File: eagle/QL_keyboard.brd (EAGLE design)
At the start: 66 x 51.4 mm, 40 parts, among them J1 USB-A-S, J2 AVR_SPI_PRG_6TESTPOINTS, U2 3.3V/150mA, U3 MAX3421ESMD, U4 ATMEGA328P_TQFP, U5 TXB0108PW-TSSOP20, Y1 8MHZ

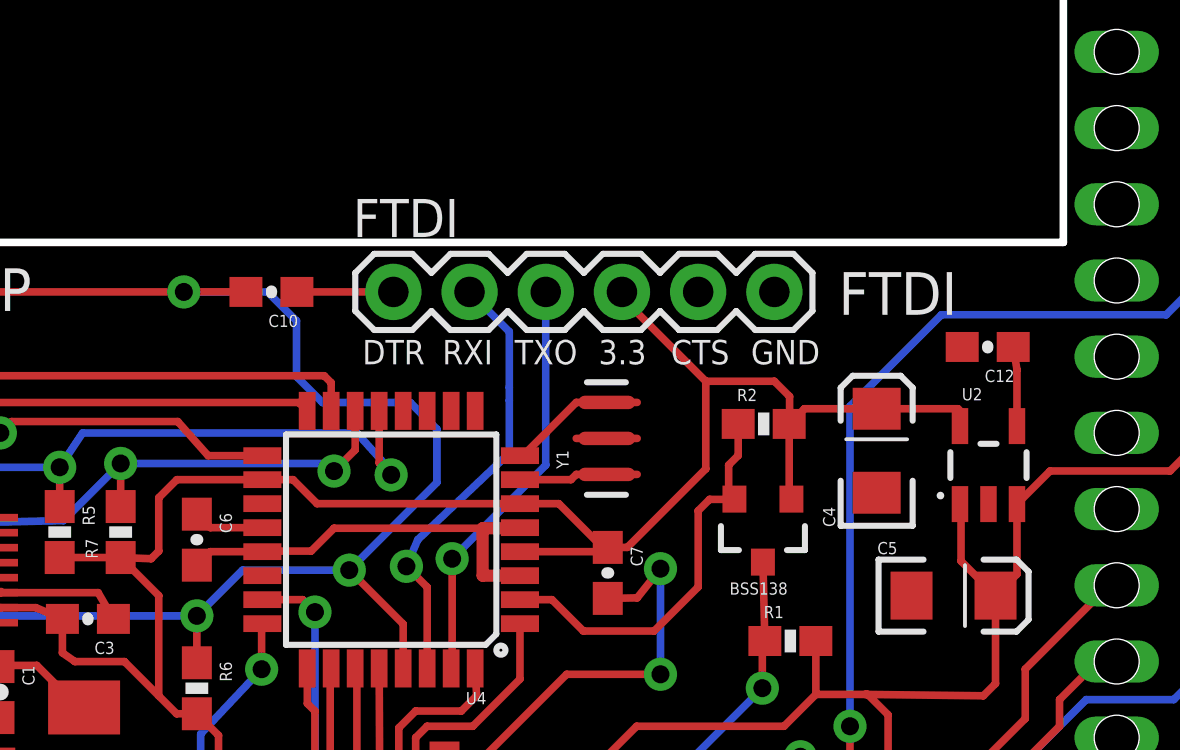
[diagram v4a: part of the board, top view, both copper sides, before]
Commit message: Replace FTDI header with a two pin RXI/TXO header.
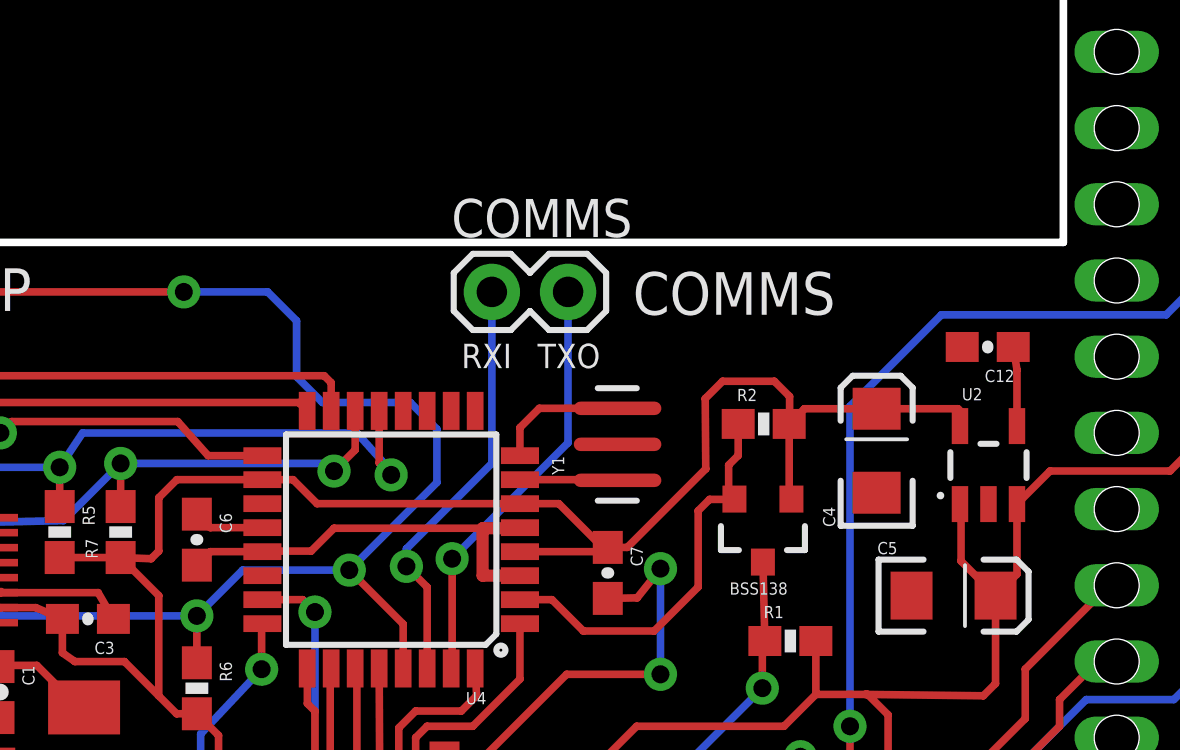
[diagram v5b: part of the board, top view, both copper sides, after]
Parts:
- removed C10: 0.1uF, SparkFun-Capacitors:0603-CAP
- removed FTDI: 1, SparkFun-Connectors:1X06
- added COMMS: (no value), ppe_custom:1X02
- Y1: device SparkFun-FreqCtrl:RESONATOR-SMD -> ppe_custom:RESONATOR-SMD
- moved Y1 0.41 mm to (46.1, 26.5)
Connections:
- removed net DTR: C10.1, FTDI.1
- net 3.3V: no longer FTDI.4
- net GND: no longer FTDI.5, FTDI.6
- net RST: no longer C10.2
- net RXI: now also COMMS.1; no longer FTDI.2
- net TXO: now also COMMS.2; no longer FTDI.3
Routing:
- net 3.3V: track 93.9 -> 89.4 mm
- net DTR: track 3.21 -> 0.00 mm
- net RST: track 57.0 -> 55.0 mm
- net N$15: track 2.61 -> 4.45 mm
- net N$16: track 1.98 -> 3.26 mm
- net RXI: track 14.8 -> 14.0 mm
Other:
- board text added: "COMMS"
- board text removed: "CTS"
- board text removed: "DTR"
- board text removed: "FTDI"

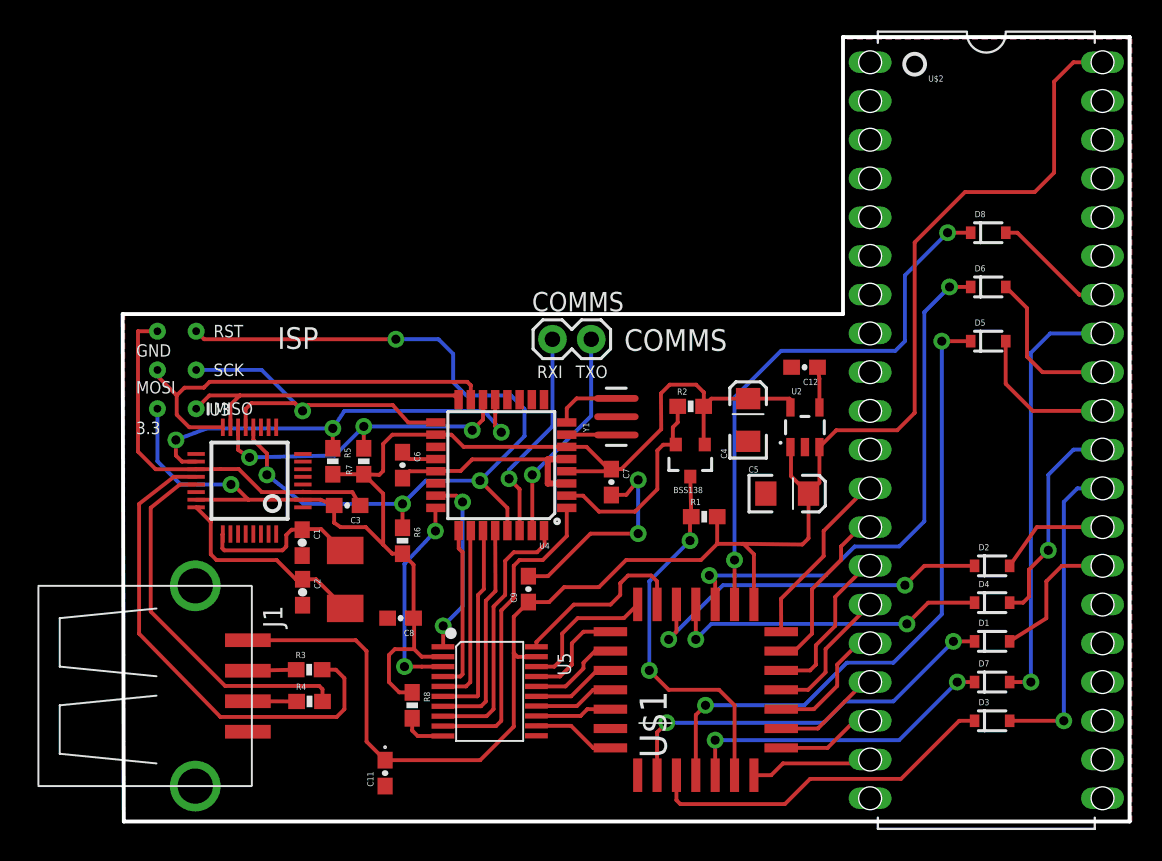
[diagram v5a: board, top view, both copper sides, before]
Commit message: Move ISP header and fix USB connector footprint
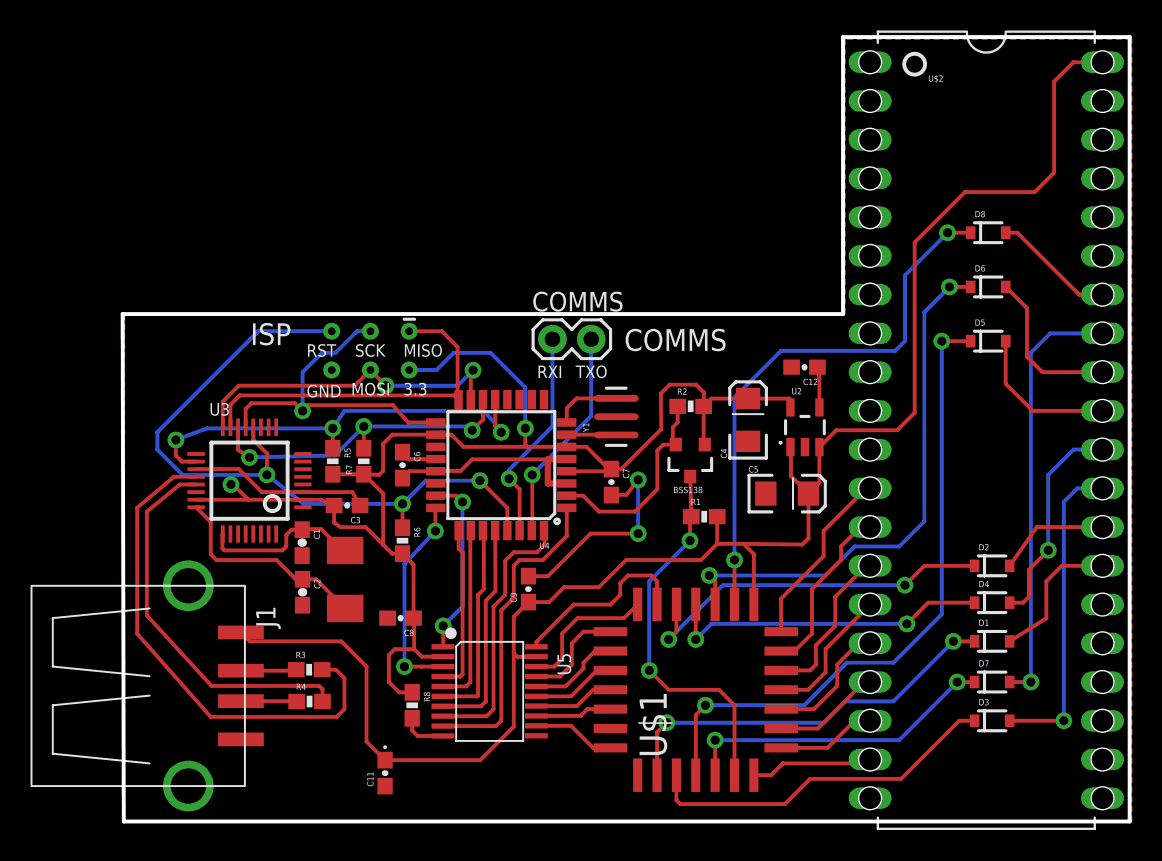
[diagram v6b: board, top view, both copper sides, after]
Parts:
- J1: device SparkFun-Connectors:USB-A-S -> ppe_custom:USB-A-S
- moved J2 12.8 mm to (30.0, 30.9), turned to 180 degrees
- moved J1 0.45 mm to (18.0, 8.89)
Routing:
- net GND: track 53.6 -> 40.2 mm
- net RST: track 55.0 -> 47.5 mm, vias 4 -> 3
- net MOSI: track 27.5 -> 21.8 mm, vias 0 -> 2
- net 3.3V: track 89.4 -> 93.5 mm, vias 1 -> 2
- net MISO: track 20.0 -> 23.9 mm
- net N$3: track 24.5 -> 25.1 mm

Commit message: General cleanup of layout
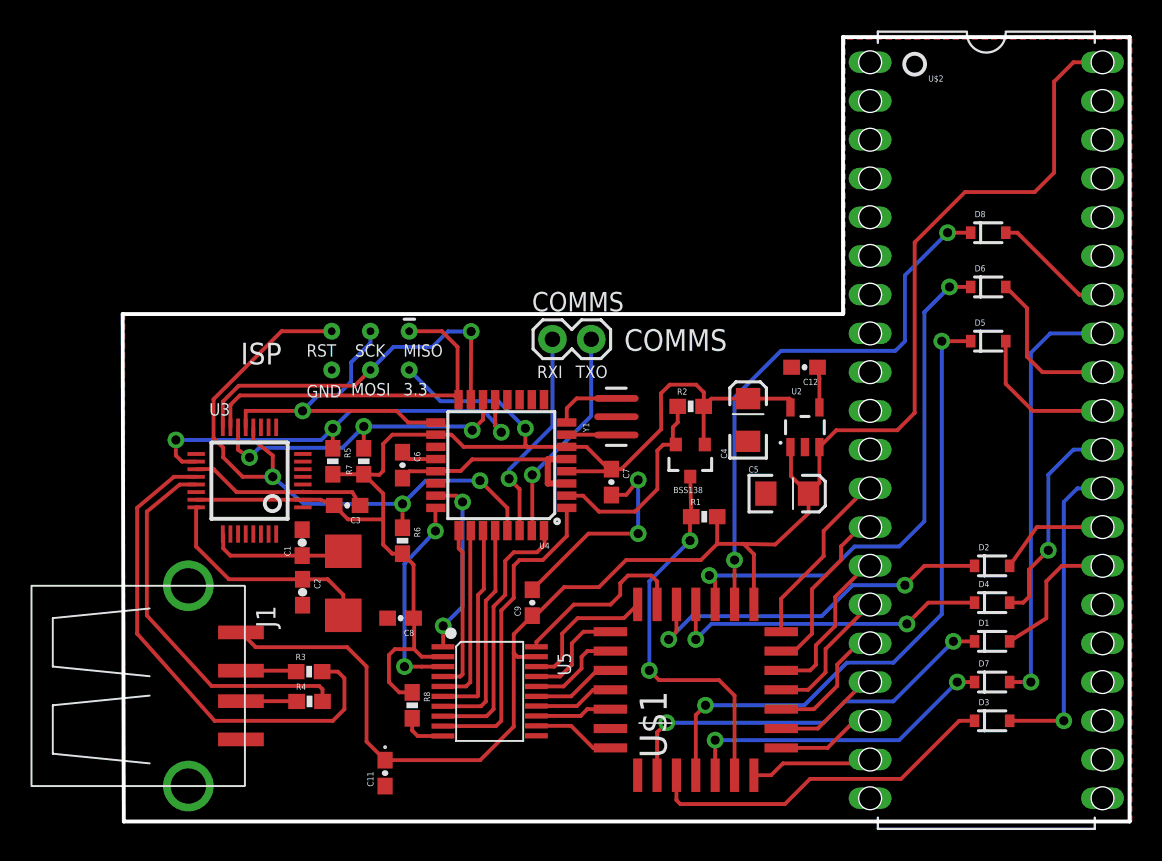
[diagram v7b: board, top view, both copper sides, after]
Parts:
- removed XTAL-12MHZ: CRYSTAL-SMD, ppe_custom:CRYSTAL-SMD-5X3.2
- added U$3: CRYSTAL-SMD, ppe_custom:CRYSTAL-SMD-5X3.2
- moved C9 0.92 mm to (40.6, 14.3)
- moved R3 0.13 mm to (26.0, 9.83)
- turned C1 to 90 degrees
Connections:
- net MAX_X0: now also U$3.1; no longer XTAL-12MHZ.1
- net MAX_X1: now also U$3.2; no longer XTAL-12MHZ.2
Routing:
- net RST: track 47.5 -> 41.8 mm
- net 3.3V: track 93.5 -> 88.1 mm, vias 2 -> 1
- net MOSI: track 21.8 -> 24.4 mm, vias 2 -> 1
- net VCC: track 111.4 -> 109.7 mm
- net MAX_X0: track 10.7 -> 9.14 mm
- net SCK: track 22.8 -> 21.7 mm
- net MAX_X1: track 14.0 -> 15.1 mm
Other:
- board text added: "USB Keyboard Adapter For the Sinclair QL (c) 2016 Petri Pellinen https://github.com/ppe/QL_USB_Keyboard v 0.3"
- board text removed: "USB Keyboard Adapter For the Sinclair QL (c) 2016 Petri Pellinen https://github.com/ppe/QL_USB_Keyboard v 0.2"

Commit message: Add QL reset logic with voltage level shifting.
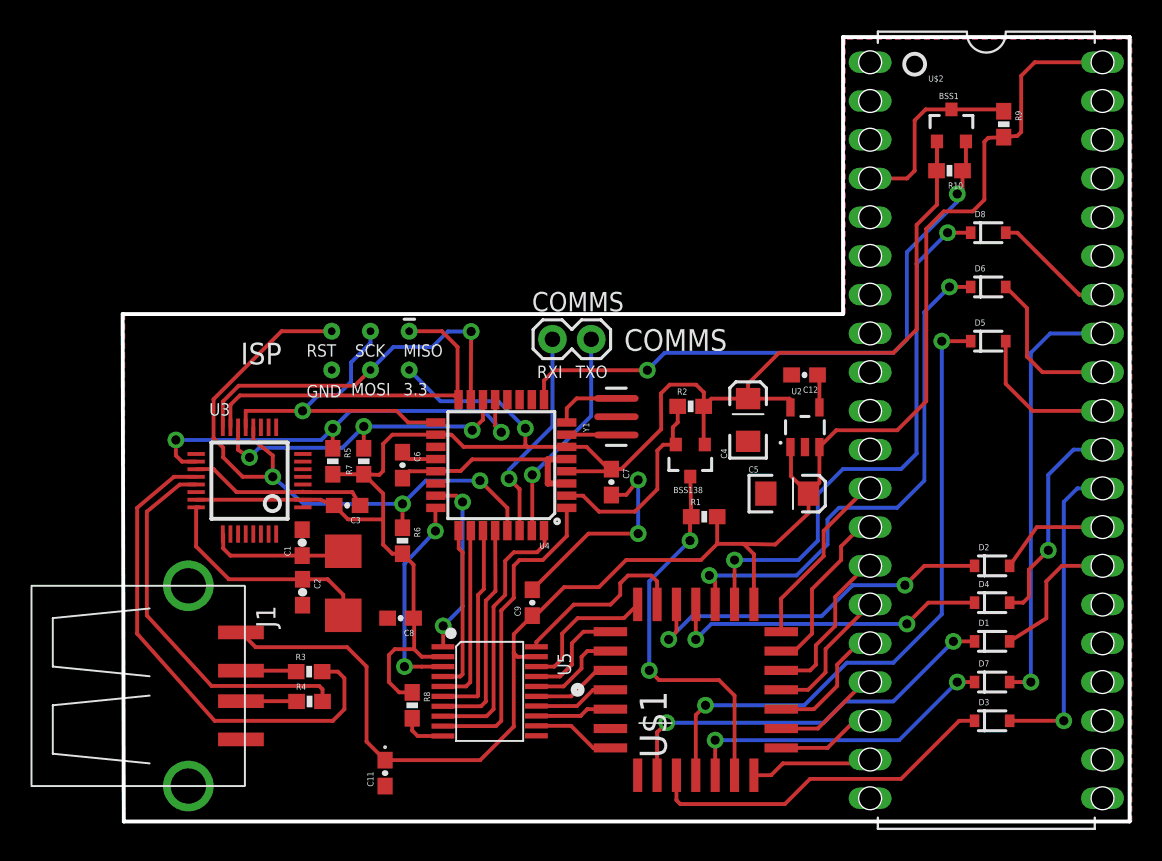
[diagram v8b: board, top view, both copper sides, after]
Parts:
- added BSS1: 200mA/50V, SparkFun-DiscreteSemi:SOT23-3
- added R10, R9: 10K, SparkFun-Resistors:0603-RES
- moved C12 0.51 mm to (58.4, 29.3)
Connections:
- new net RSTQL: BSS1.3, R9.1, U$2.4
- new net RSTQLV33: BSS1.2, R10.1, U4.9
- net 3.3V: now also BSS1.1, R10.2
- net VCC: now also R9.2
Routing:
- net RSTQLV33: track 0.00 -> 40.7 mm, vias 0 -> 2
- net 3.3V: track 88.1 -> 116.4 mm
- net RSTQL: track 0.00 -> 12.6 mm
- net VCC: track 109.7 -> 110.6 mm
- net N$24: track 35.1 -> 34.5 mm
